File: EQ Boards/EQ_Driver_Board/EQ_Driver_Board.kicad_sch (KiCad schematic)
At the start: 24 parts, among them Q1 MPSA63, Q2 MPSA70, Q3 MPSA70, Q4 MPSA20

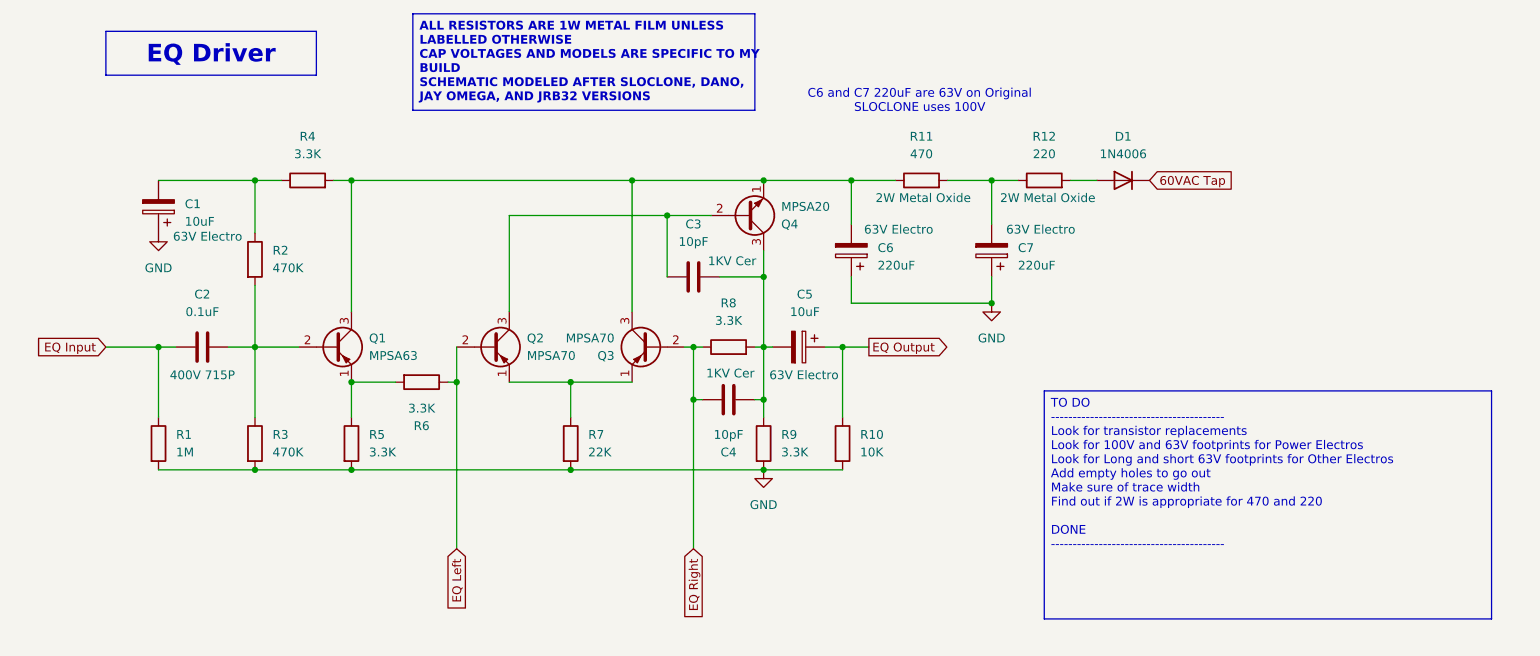
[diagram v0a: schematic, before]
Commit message: Updated Schematics and Organizational Structure
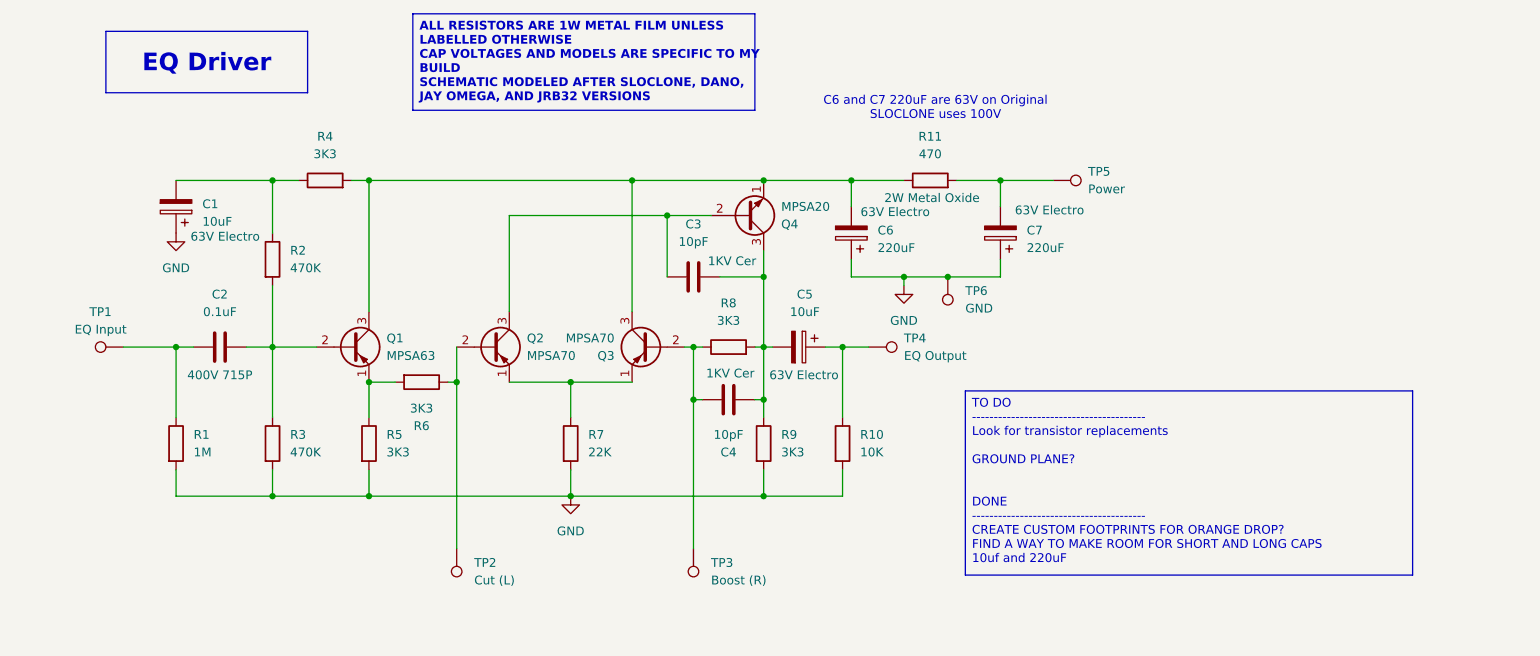
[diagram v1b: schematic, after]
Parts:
- removed D1: 1N4006, Diode_THT:D_DO-41_SOD81_P10.16mm_Horizontal, symbol Diode:1N4006
- removed R12: 220, symbol Device:R
- added TP1: EQ Input, HiroFootprints:Out_Hole_3.4_1.8, symbol Connector:TestPoint
- added TP2: Cut (L), HiroFootprints:Out_Hole_3.4_1.8, symbol Connector:TestPoint
- added TP3: Boost (R), HiroFootprints:Out_Hole_3.4_1.8, symbol Connector:TestPoint
- added TP4: EQ Output, HiroFootprints:Out_Hole_3.4_1.8, symbol Connector:TestPoint
- added TP5: Power, HiroFootprints:Out_Hole_3.4_1.8, symbol Connector:TestPoint
- added TP6: GND, HiroFootprints:Out_Hole_3.4_1.8, symbol Connector:TestPoint
- C1, C5: footprint (none) -> Capacitor_THT:CP_Axial_L18.0mm_D6.5mm_P25.00mm_Horizontal
- C2: footprint (none) -> HiroFootprints:715P10454LAD3
- C3, C4: footprint (none) -> Capacitor_THT:C_Rect_L11.0mm_W3.5mm_P10.00mm_MKT
- C6, C7: footprint (none) -> Capacitor_THT:CP_Axial_L25.0mm_D10.0mm_P30.00mm_Horizontal
- Q1, Q2, Q3, Q4: footprint Package_TO_SOT_THT:TO-92_Inline -> Package_TO_SOT_THT:TO-92_Wide
- R1, R10, R11, R2, R3, R7: footprint (none) -> Resistor_THT:R_Axial_DIN0411_L9.9mm_D3.6mm_P15.24mm_Horizontal
- R4, R5, R6, R8, R9: value 3.3K -> 3K3; footprint (none) -> Resistor_THT:R_Axial_DIN0411_L9.9mm_D3.6mm_P15.24mm_Horizontal
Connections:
- net GND: now also TP6.1
- net at C7.2, R11.2: now also TP5.1
- net EQ Input: no longer names the net of C2.1, R1.1
- net EQ Input: now also TP1.1
- net EQ Left: no longer names the net of Q2.2 (B), R6.1
- net EQ Left: now also TP2.1
- net EQ Output: no longer names the net of C5.1, R10.1
- net EQ Output: now also TP4.1
- net EQ Right: no longer names the net of C4.1, Q3.2 (B), R8.1
- net EQ Right: now also TP3.1
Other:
- moved on the sheet: C1, C2, C6, C7, Q1, R1, R11, R2, R3, R4, R5
